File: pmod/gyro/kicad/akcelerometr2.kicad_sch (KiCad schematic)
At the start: 5 parts, among them J2 Conn_01x04_Pin, J3 Conn_01x04_Pin, J4 Conn_01x08_Pin

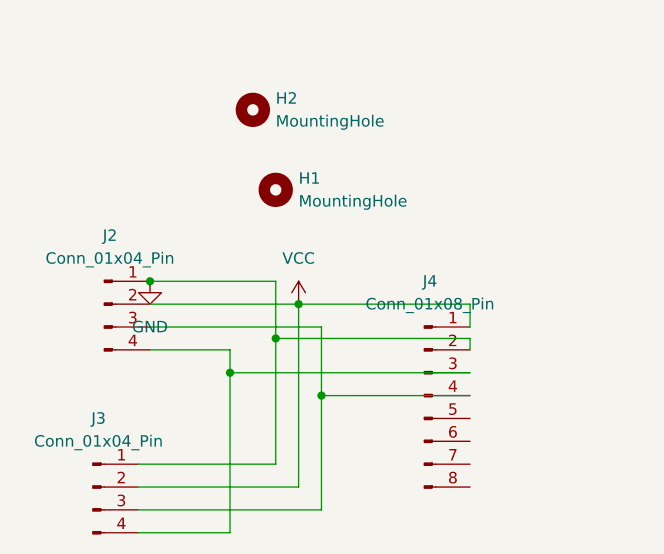
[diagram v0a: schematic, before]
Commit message: Oprava v modulu gyro
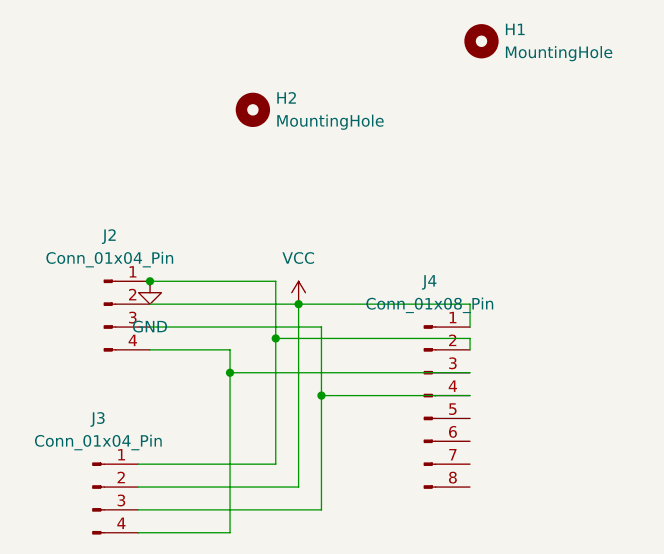
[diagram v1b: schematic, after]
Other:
- moved on the sheet: H1
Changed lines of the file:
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@@
 	(symbol
 		(lib_id "Mechanical:MountingHole")
-		(at 130.81 53.34 0)
+		(at 153.67 36.83 0)
 		(unit 1)
 		(exclude_from_sim no)
@@
 		(fields_autoplaced yes)
 		(property "Reference" "H1"
-			(at 133.35 52.0699 0)
+			(at 156.21 35.5599 0)
 			(effects
 				(font
@@
 		)
 		(property "Value" "MountingHole"
-			(at 133.35 54.6099 0)
+			(at 156.21 38.0999 0)
 			(effects
 				(font
@@
 		)
 		(property "Footprint" "MountingHole:MountingHole_3.2mm_M3"
-			(at 130.81 53.34 0)
+			(at 153.67 36.83 0)
 			(effects
 				(font
@@
 		)
 		(property "Datasheet" "~"
-			(at 130.81 53.34 0)
+			(at 153.67 36.83 0)
 			(effects
 				(font
@@
 		)
 		(property "Description" "Mounting Hole without connection"
-			(at 130.81 53.34 0)
+			(at 153.67 36.83 0)
 			(effects
 				(font
